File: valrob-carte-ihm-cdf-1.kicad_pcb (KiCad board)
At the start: 2 copper layers, 75 parts, among them J1 USB_C_Receptacle_USB2.0_14P, J2 Conn_01x02, J3 Conn_01x02, J4 Conn_01x04_Pin, J5 Conn_01x04_Pin, J6 Conn_01x04_Pin, SW1 SW_Push, SW2 SW_Push, SW3 SW_DIP_x04, SW4 SW_SPDT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

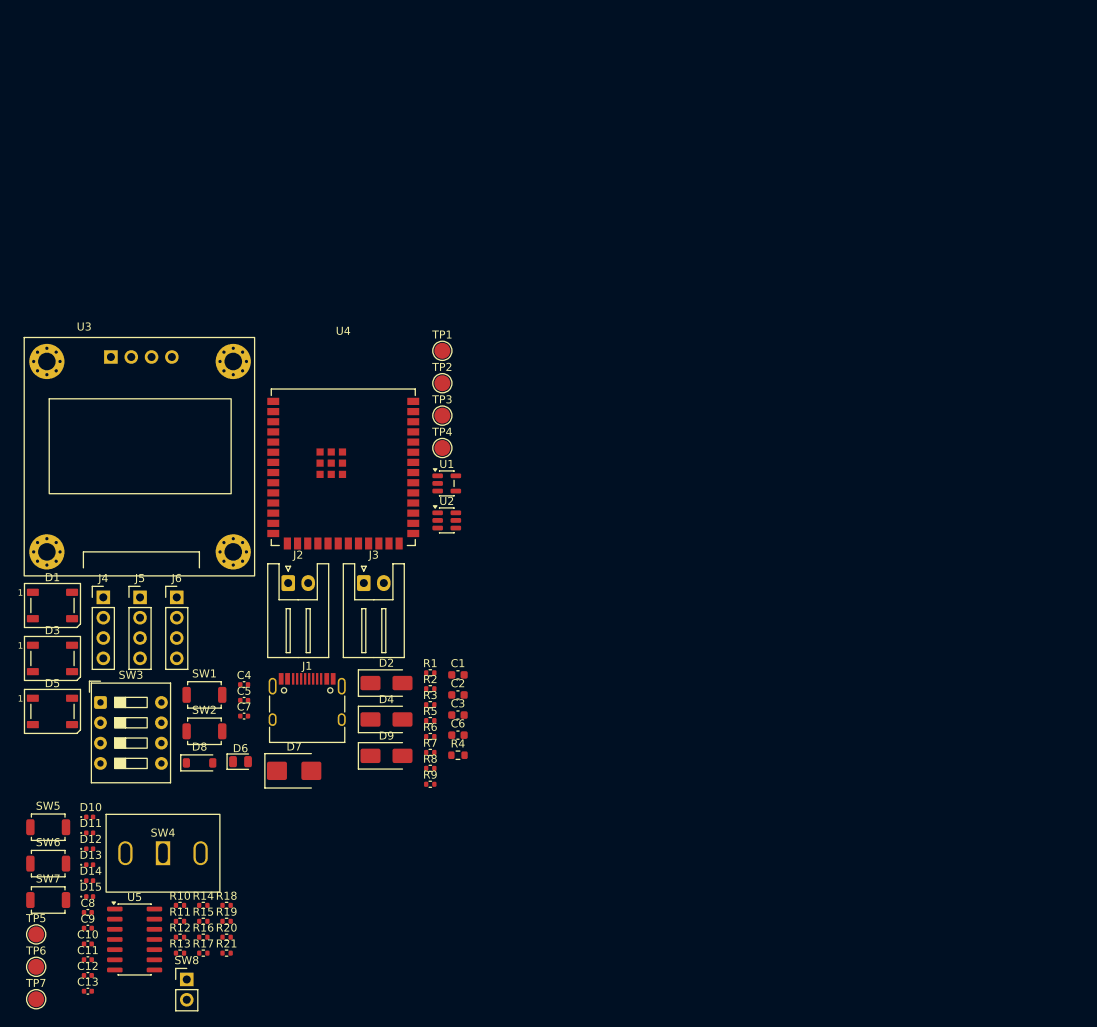
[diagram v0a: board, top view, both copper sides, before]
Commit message: pcb: add initial rough placement
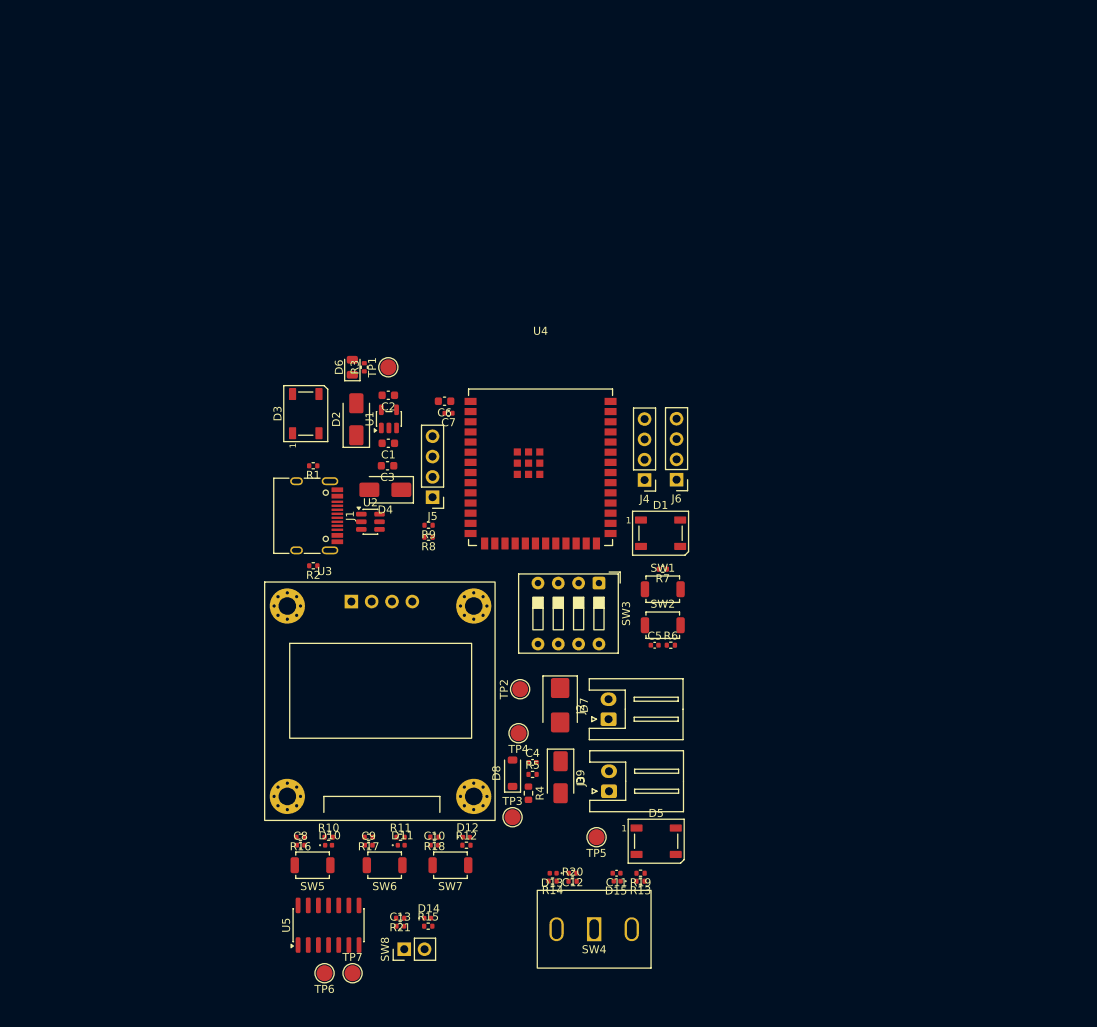
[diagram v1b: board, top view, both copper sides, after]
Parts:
- moved D5 77.2 mm to (121.0, 163.0)
- moved D1 76.5 mm to (121.5, 124.5)
- moved TP5 71.1 mm to (113.5, 162.5), turned to 180 degrees
- moved J4 69.2 mm to (119.5, 117.8), turned to 180 degrees
- moved C11 67.0 mm to (116.0, 167.0), turned to 180 degrees
- moved D15 66.0 mm to (116.1, 168.0), turned to 180 degrees
- moved J6 64.2 mm to (123.5, 117.8), turned to 180 degrees
- moved SW3 64.1 mm to (113.8, 130.7), turned to -90 degrees
- moved C12 61.9 mm to (110.5, 167.0), turned to 180 degrees
- moved SW2 58.8 mm to (121.8, 136.0)
- moved SW1 58.8 mm to (121.8, 131.5)
- moved R13 58.3 mm to (119.0, 168.0), turned to 180 degrees
- moved D13 57.9 mm to (108.1, 167.0), turned to 180 degrees
- moved SW4 54.7 mm to (113.2, 174.0), turned to 180 degrees
- moved R19 52.1 mm to (119.0, 167.0), turned to 180 degrees
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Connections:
- SW3 pad 2: Net-(U4-GPIO46) -> Net-(U4-GPIO48/SPICLK_N/SUBSPICLK_N_DIFF)
- SW3 pad 4: Net-(U4-GPIO48/SPICLK_N/SUBSPICLK_N_DIFF) -> Net-(U4-GPIO21)
- U4 pad 16: Net-(U4-GPIO46) -> unconnected-(U4-GPIO46-Pad16)
- U4 pad 23: unconnected-(U4-GPIO21-Pad23) -> Net-(U4-GPIO21)

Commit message: pcb: add layout refinement and board outline
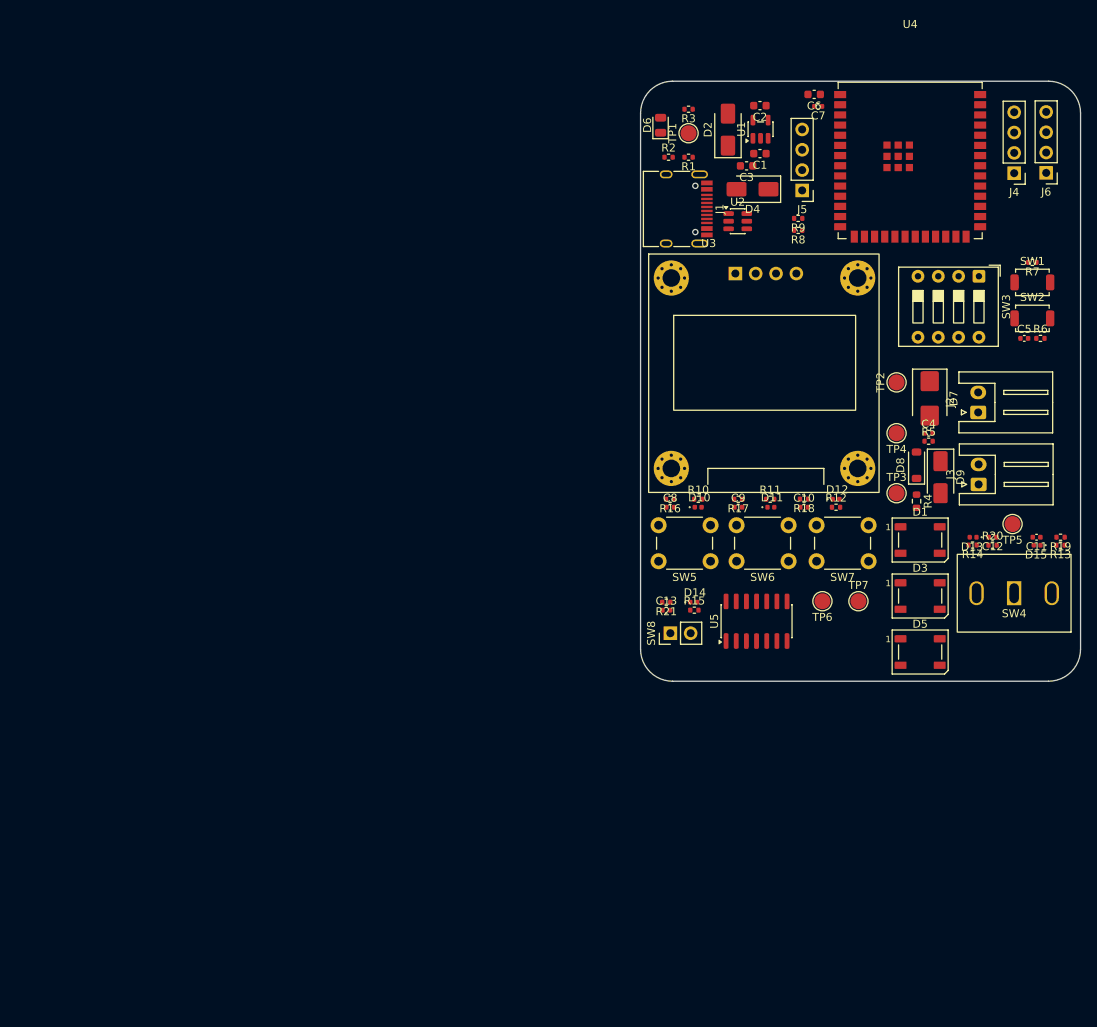
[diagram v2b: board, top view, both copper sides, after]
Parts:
- SW5, SW6, SW7: footprint Button_Switch_SMD:SW_SPST_TS-1088-xR020 -> Button_Switch_THT:SW_PUSH_6mm_H7.3mm
- moved D3 80.1 mm to (153.9, 132.3), turned to 0 degrees
- moved TP7 78.5 mm to (146.2, 133.0)
- moved TP6 77.7 mm to (141.7, 133.0)
- moved R2 67.7 mm to (122.5, 77.5), turned to 0 degrees
- moved R13 67.2 mm to (171.5, 126.0)
- moved C11 67.2 mm to (168.5, 125.0)
- moved C12 67.2 mm to (163.0, 125.0)
- moved D13 67.2 mm to (160.6, 125.0)
- moved D15 67.2 mm to (168.6, 126.0)
- moved R14 67.2 mm to (160.5, 126.0)
- moved R19 67.2 mm to (171.5, 125.0)
- moved R20 67.2 mm to (163.0, 126.0)
- moved SW4 67.2 mm to (165.7, 132.0)
- moved U5 65.6 mm to (133.5, 135.5)
- moved TP5 65.1 mm to (165.5, 123.4)
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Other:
- board outline added: 55 x 75 mm

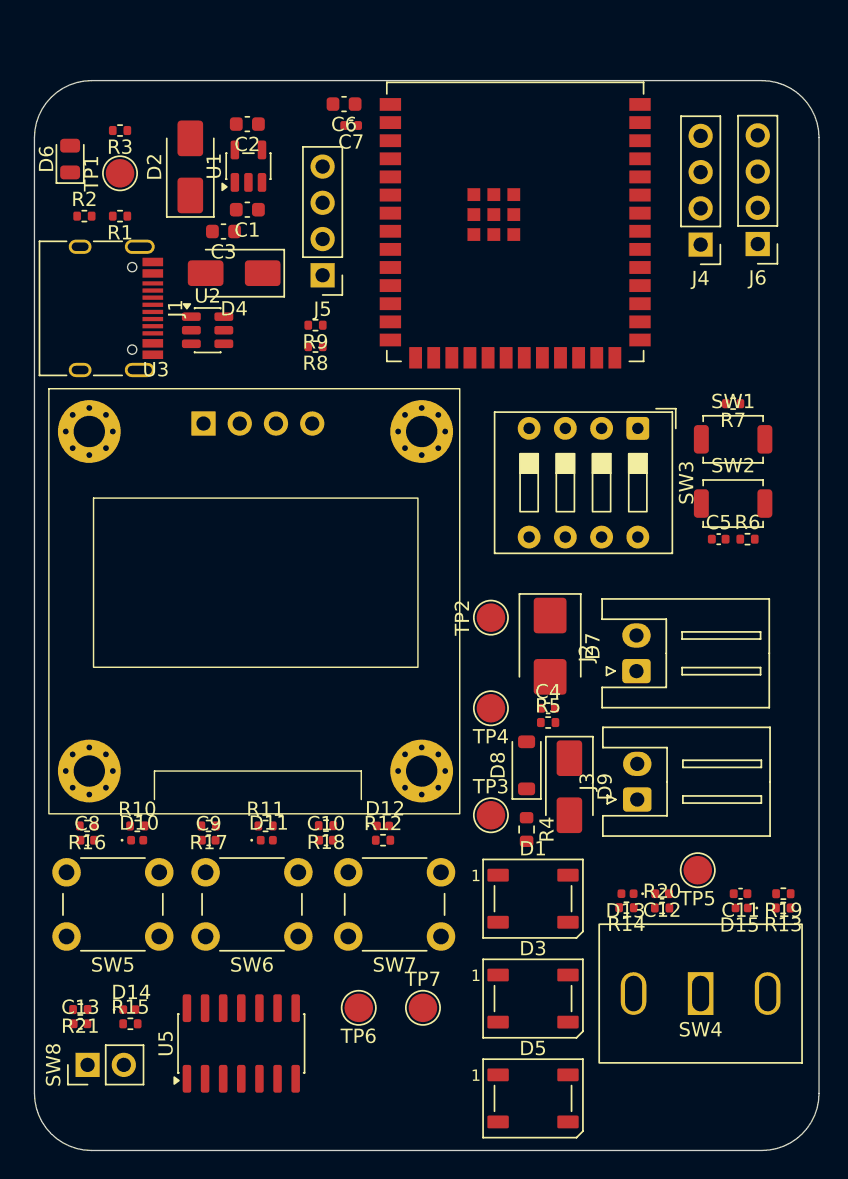
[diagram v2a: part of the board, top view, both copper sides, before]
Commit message: pcb: add M2 mounting holes
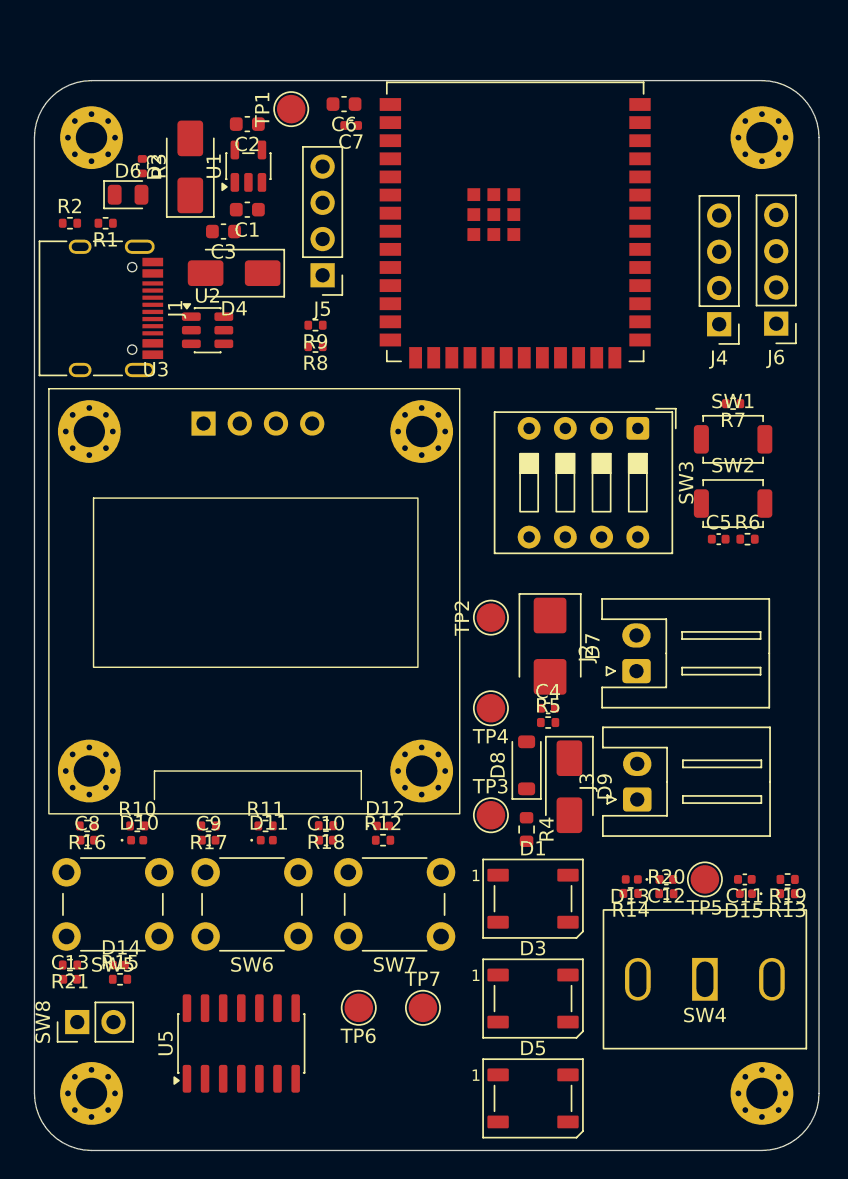
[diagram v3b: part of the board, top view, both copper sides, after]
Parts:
- added REF**: MountingHole_2.2mm_M2_Pad_Via, MountingHole:MountingHole_2.2mm_M2_Pad_Via, F.Cu at (170.0, 139.0)
- added REF**: MountingHole_2.2mm_M2_Pad_Via, MountingHole:MountingHole_2.2mm_M2_Pad_Via, F.Cu at (170.0, 72.0)
- added REF**: MountingHole_2.2mm_M2_Pad_Via, MountingHole:MountingHole_2.2mm_M2_Pad_Via, F.Cu at (123.0, 72.0)
- added REF**: MountingHole_2.2mm_M2_Pad_Via, MountingHole:MountingHole_2.2mm_M2_Pad_Via, F.Cu at (123.0, 139.0)
- moved TP1 12.8 mm to (137.0, 70.0)
- moved J6 5.73 mm to (171.0, 85.0)
- moved J4 5.73 mm to (167.0, 85.1)
- moved D6 4.77 mm to (125.6, 76.0), turned to 0 degrees
- moved D14 3.20 mm to (124.9, 130.0)
- moved R21 3.20 mm to (121.5, 130.0)
- moved C13 3.20 mm to (121.5, 131.0)
- moved R15 3.20 mm to (125.0, 131.0)
- moved SW8 3.09 mm to (122.0, 134.0)
- moved R3 2.95 mm to (126.6, 74.0), turned to -90 degrees
- moved R1 1.13 mm to (124.0, 78.0)
- moved R2 1.13 mm to (121.5, 78.0)
- moved C11 1.04 mm to (168.8, 124.0)
- moved C12 1.04 mm to (163.3, 124.0)
- moved D13 1.04 mm to (160.9, 124.0)
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
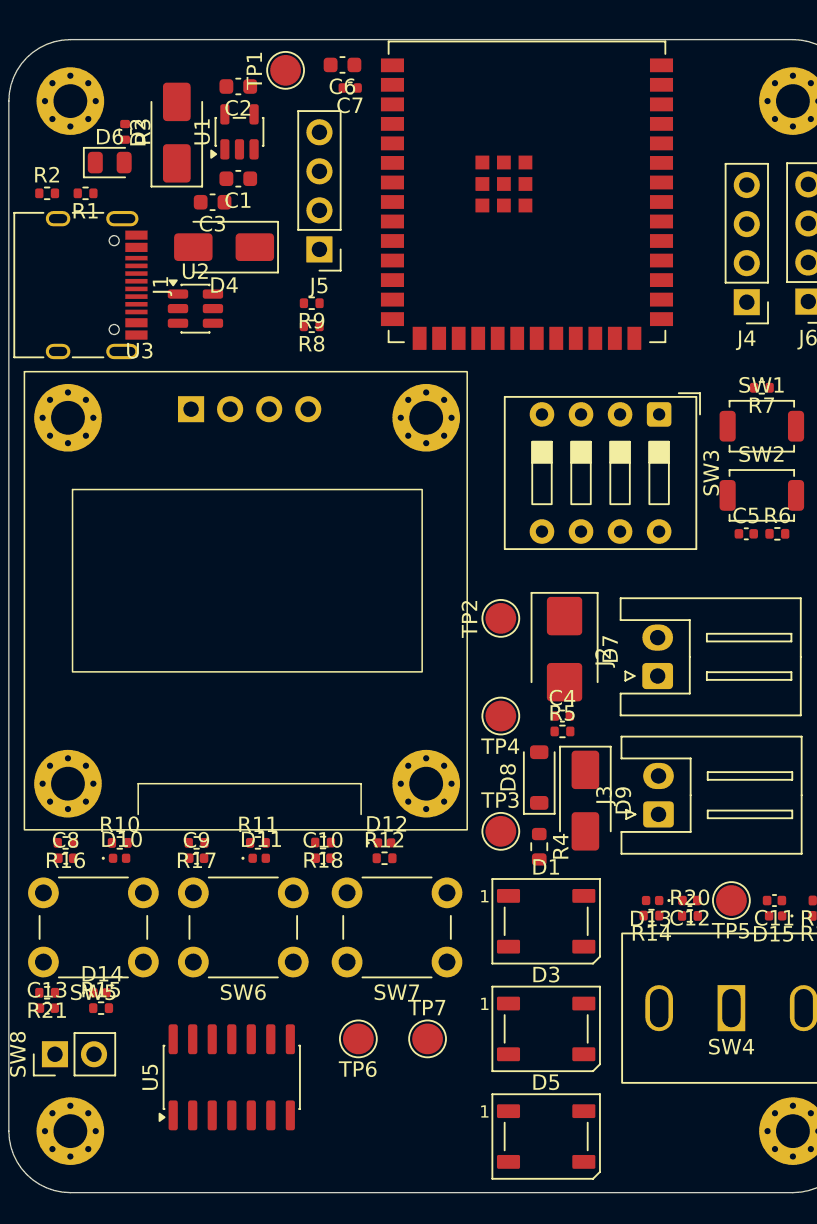
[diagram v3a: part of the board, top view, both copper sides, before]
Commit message: pcb: add fiducials and tooling holes
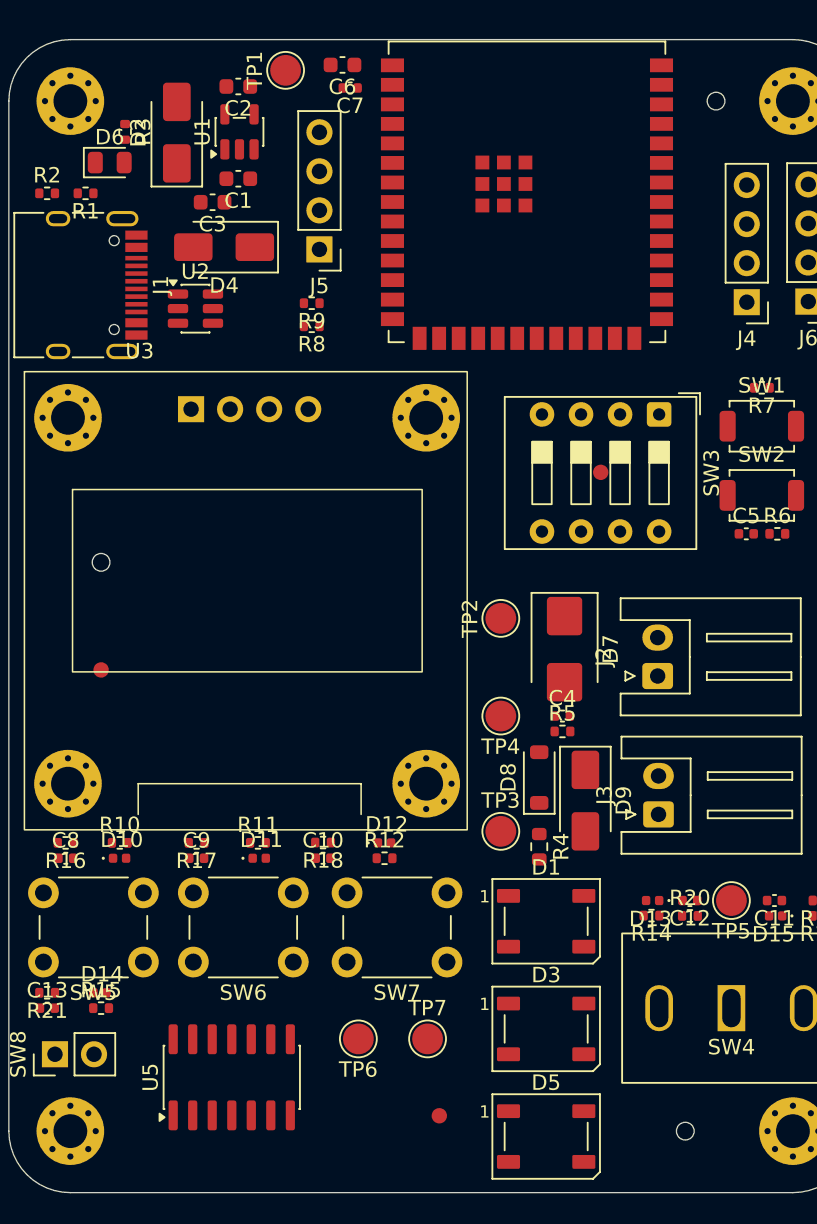
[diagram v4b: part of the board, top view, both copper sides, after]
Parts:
- added REF**: ToolingHole_1.152mm, MountingHole:ToolingHole_1.152mm, F.Cu at (165.0, 72.0)
- added REF**: ToolingHole_1.152mm, MountingHole:ToolingHole_1.152mm, F.Cu at (163.0, 139.0)
- added REF**: Fiducial_1mm_Mask2mm, Fiducial:Fiducial_1mm_Mask2mm, F.Cu at (147.0, 138.0)
- added REF**: ToolingHole_1.152mm, MountingHole:ToolingHole_1.152mm, F.Cu at (125.0, 102.0)
- added REF**: Fiducial_1mm_Mask2mm, Fiducial:Fiducial_1mm_Mask2mm, F.Cu at (125.0, 109.0)
- added REF**: Fiducial_1mm_Mask2mm, Fiducial:Fiducial_1mm_Mask2mm, F.Cu at (157.5, 96.1)
